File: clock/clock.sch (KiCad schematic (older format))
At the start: 3 parts

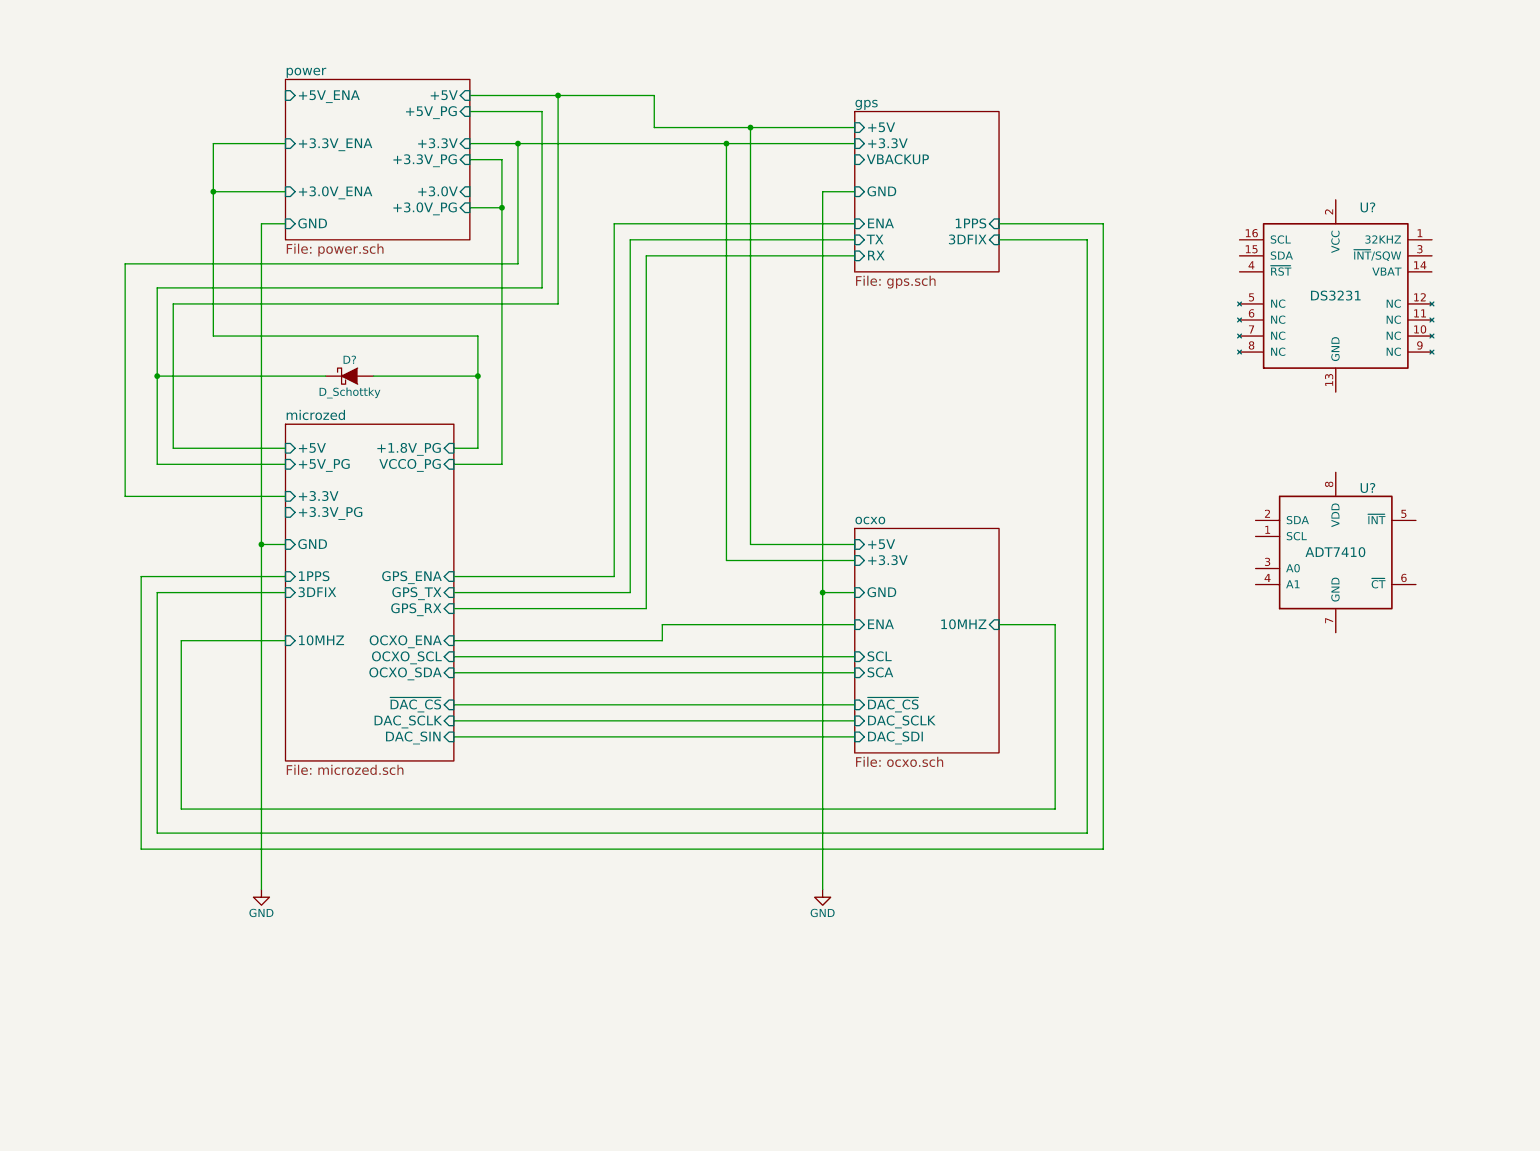
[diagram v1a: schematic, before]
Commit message: Add parameter for RF connector. Start adding display connections.
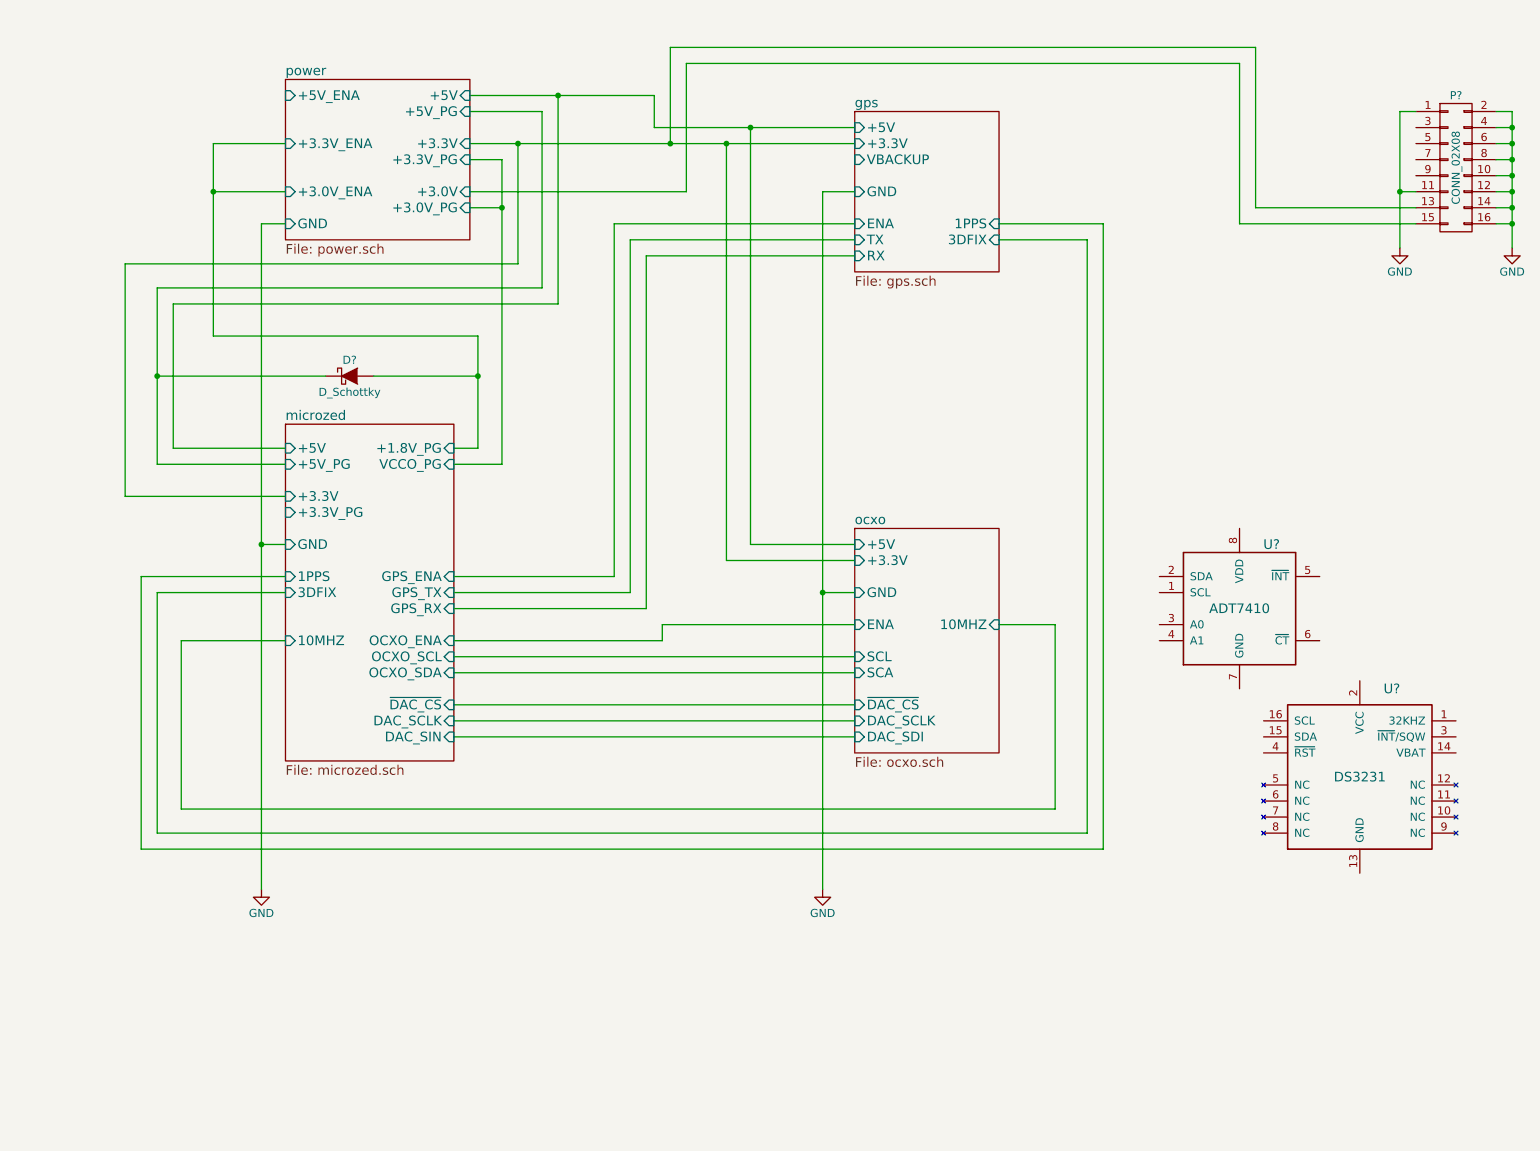
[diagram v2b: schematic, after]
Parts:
- removed U?: DS3231, symbol DS3231
- removed U?: ADT7410, symbol ADT7410
- added P?: CONN_02X08, symbol CONN_02X08
- added U?: DS3231, symbol DS3231
- added U?: ADT7410, symbol ADT7410
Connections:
- net GND: now also P?.1 (P1), P?.10 (P10), P?.11 (P11), P?.12 (P12), P?.14 (P14), P?.16 (P16), P?.2 (P2), P?.4 (P4), P?.6 (P6), P?.8 (P8)
- net gps/+3.3V: now also P?.13 (P13)
- net power/+3.0V: now also P?.15 (P15)
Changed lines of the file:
@@
 F10 "ENA" I L 5950 1800 60
 $EndSheet
-$Comp
-L DS3231 U?
-U 1 1 56133FFE
-P 8950 2250
-F 0 "U?" H 9150 2800 60  0000 C CNN
-F 1 "DS3231" H 8950 2250 60  0000 C CNN
-F 2 "" H 8950 2300 60  0000 C CNN
-F 3 "" H 8950 2300 60  0000 C CNN
-	1    8950 2250
-	1    0    0    -1
-$EndComp
-$Comp
-L ADT7410 U?
-U 1 1 56134604
-P 8950 3850
-F 0 "U?" H 9150 4250 60  0000 C CNN
-F 1 "ADT7410" H 8950 3850 60  0000 C CNN
-F 2 "" H 8950 3800 60  0000 C CNN
-F 3 "" H 8950 3800 60  0000 C CNN
-	1    8950 3850
-	1    0    0    -1
-$EndComp
 $Sheet
 S 2400 3050 1050 2100
@@
 $EndSheet
 Wire Wire Line
-	3550 1000 4700 1000
+	3550 1000 4100 1000
+Wire Wire Line
+	4100 1000 4700 1000
 Wire Wire Line
 	4100 1000 4100 2300
@@
 	4000 1100 4000 2200
 Wire Wire Line
-	1950 1300 1950 2500
+	1950 1300 1950 1600
+Wire Wire Line
+	1950 1600 1950 2500
 Wire Wire Line
 	1950 1300 2400 1300
@@
 	1750 4400 2400 4400
 Wire Wire Line
-	4700 1000 4700 1200
-Wire Wire Line
-	4700 1200 5950 1200
+	4700 1200 5300 1200
+Wire Wire Line
+	5300 1200 5950 1200
 Connection ~ 4100 1000
 Wire Wire Line
-	3550 1300 5950 1300
+	3550 1300 3850 1300
+Wire Wire Line
+	3850 1300 4800 1300
+Wire Wire Line
+	4800 1300 5150 1300
+Wire Wire Line
+	5150 1300 5950 1300
 Wire Wire Line
 	5300 1200 5300 3800
@@
 	2400 3800 2250 3800
 Wire Wire Line
-	2250 1800 2250 5950
+	2250 1800 2250 3800
+Wire Wire Line
+	2250 3800 2250 5950
 Wire Wire Line
 	5950 1600 5750 1600
 Wire Wire Line
-	5750 1600 5750 5950
+	5750 1600 5750 4100
+Wire Wire Line
+	5750 4100 5750 5950
 Wire Wire Line
 	2400 1800 2250 1800
@@
 	3550 1400 3750 1400
 Wire Wire Line
-	3750 1400 3750 3300
+	3750 1400 3750 1700
+Wire Wire Line
+	3750 1700 3750 3300
 Wire Wire Line
 	3750 3300 3450 3300
@@
 	3450 3200 3600 3200
 Wire Wire Line
-	3600 3200 3600 2500
+	3600 3200 3600 2750
+Wire Wire Line
+	3600 2750 3600 2500
 Wire Wire Line
 	3600 2500 1950 2500
@@
 	4000 2200 1600 2200
 Wire Wire Line
-	1600 2200 1600 3300
+	1600 2200 1600 2750
+Wire Wire Line
+	1600 2750 1600 3300
 Wire Wire Line
 	1600 3300 2400 3300
@@
 F11 "GND" I L 2400 1800 60
 $EndSheet
+$Comp
+L CONN_02X08 P?
+U 1 1 5632C7F9
+P 9700 1450
+F 0 "P?" H 9700 1900 50  0000 C CNN
+F 1 "CONN_02X08" V 9700 1450 50  0000 C CNN
+F 2 "" H 9700 250 60  0000 C CNN
+F 3 "" H 9700 250 60  0000 C CNN
+	1    9700 1450
+	1    0    0    -1
+$EndComp
+$Comp
+L GND #PWR?
+U 1 1 5632D32A
+P 10050 1950
+F 0 "#PWR?" H 10050 1700 50  0001 C CNN
+F 1 "GND" H 10050 1800 50  0000 C CNN
+F 2 "" H 10050 1950 60  0000 C CNN
+F 3 "" H 10050 1950 60  0000 C CNN
+	1    10050 1950
+	1    0    0    -1
+$EndComp
+Wire Wire Line
+	9950 1100 10050 1100
+Wire Wire Line
+	10050 1100 10050 1200
+Wire Wire Line
+	10050 1200 10050 1300
+Wire Wire Line
+	10050 1300 10050 1400
+Wire Wire Line
+	10050 1400 10050 1500
+Wire Wire Line
+	10050 1500 10050 1600
+Wire Wire Line
+	10050 1600 10050 1700
+Wire Wire Line
+	10050 1700 10050 1800
+Wire Wire Line
+	10050 1800 10050 1950
+Wire Wire Line
+	9950 1800 10050 1800
+Connection ~ 10050 1800
+Wire Wire Line
+	9950 1700 10050 1700
+Connection ~ 10050 1700
+Wire Wire Line
+	9950 1600 10050 1600
+Connection ~ 10050 1600
+Wire Wire Line
+	9950 1500 10050 1500
+Connection ~ 10050 1500
+Wire Wire Line
+	9950 1400 10050 1400
+Connection ~ 10050 1400
+Wire Wire Line
+	9950 1300 10050 1300
+Connection ~ 10050 1300
+Wire Wire Line
+	9950 1200 10050 1200
+Connection ~ 10050 1200
+$Comp
+L GND #PWR?
+U 1 1 5632E81A
+P 9350 1950
+F 0 "#PWR?" H 9350 1700 50  0001 C CNN
+F 1 "GND" H 9350 1800 50  0000 C CNN
+F 2 "" H 9350 1950 60  0000 C CNN
+F 3 "" H 9350 1950 60  0000 C CNN
+	1    9350 1950
+	1    0    0    -1
+$EndComp
+Wire Wire Line
+	9450 1100 9350 1100
+Wire Wire Line
+	9350 1100 9350 1600
+Wire Wire Line
+	9350 1600 9350 1950
+Wire Wire Line
+	9450 1600 9350 1600
+Connection ~ 9350 1600
+$Comp
+L DS3231 U?
+U 1 1 563309E4
+P 9100 5250
+F 0 "U?" H 9300 5800 60  0000 C CNN
+F 1 "DS3231" H 9100 5250 60  0000 C CNN
+F 2 "" H 9100 5300 60  0000 C CNN
+F 3 "" H 9100 5300 60  0000 C CNN
+F 4 "Maxim Integrated" H 9100 5325 50  0001 C CNN "Manufacturer"
+F 5 "DS3231S#" H 9100 5175 50  0001 C CNN "PartNum"
+	1    9100 5250
+	1    0    0    -1
+$EndComp
+$Comp
+L ADT7410 U?
+U 1 1 56330BE2
+P 8350 4200
+F 0 "U?" H 8550 4600 60  0000 C CNN
+F 1 "ADT7410" H 8350 4200 60  0000 C CNN
+F 2 "" H 8350 4150 60  0000 C CNN
+F 3 "" H 8350 4150 60  0000 C CNN
+F 4 "Analog Devices" H 8700 4775 50  0001 C CNN "Manufacturer"
+F 5 "ADT7410TRZ" H 8650 4700 50  0001 C CNN "PartNum"
+	1    8350 4200
+	1    0    0    -1
+$EndComp
+Wire Wire Line
+	3550 1600 4900 1600
+Wire Wire Line
+	4900 1600 4900 800
+Wire Wire Line
+	4900 800  8350 800
+Wire Wire Line
+	8350 800  8350 1800
+Wire Wire Line
+	8350 1800 9450 1800
+Wire Wire Line
+	9450 1700 8450 1700
+Wire Wire Line
+	8450 1700 8450 700
+Wire Wire Line
+	8450 700  4800 700
+Wire Wire Line
+	4700 1000 4700 1200
+Wire Wire Line
+	4800 1300 4800 700
+Connection ~ 4800 1300
 $EndSCHEMATC

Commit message: Add sheet for RTC and temperature sensors.
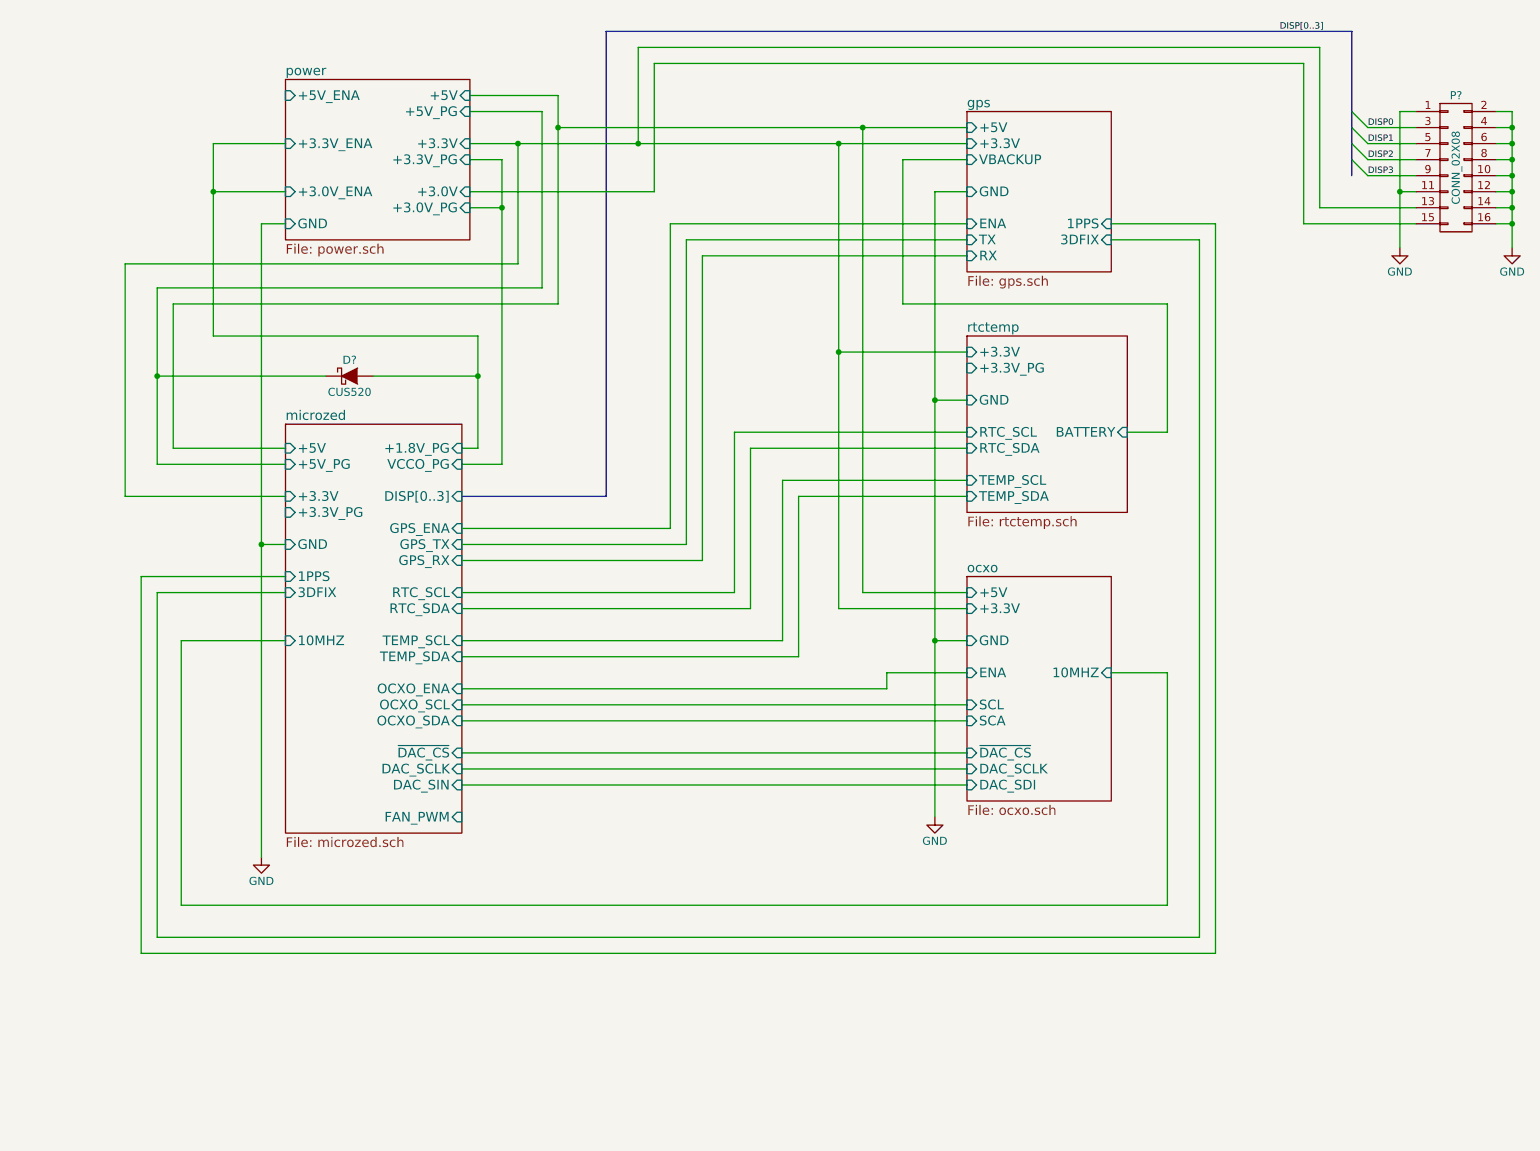
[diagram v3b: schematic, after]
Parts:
- removed U?: DS3231, symbol DS3231
- removed U?: ADT7410, symbol ADT7410
- D?: value D_Schottky -> CUS520; Manufacturer (none) -> Toshiba; PartNum (none) -> CUS520
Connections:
- net DISP0: now reaches P?.3 (P3)
- net DISP1: now reaches P?.5 (P5)
- net DISP2: now reaches P?.7 (P7)
- net DISP3: now reaches P?.9 (P9)
